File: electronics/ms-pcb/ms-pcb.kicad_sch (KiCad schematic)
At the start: 20 parts, among them J1 Left motor, J2 Right motor, J3 XT60-M, U1 ESP32-S3-DEVKITC-1U-N8R2, U2 GY-521

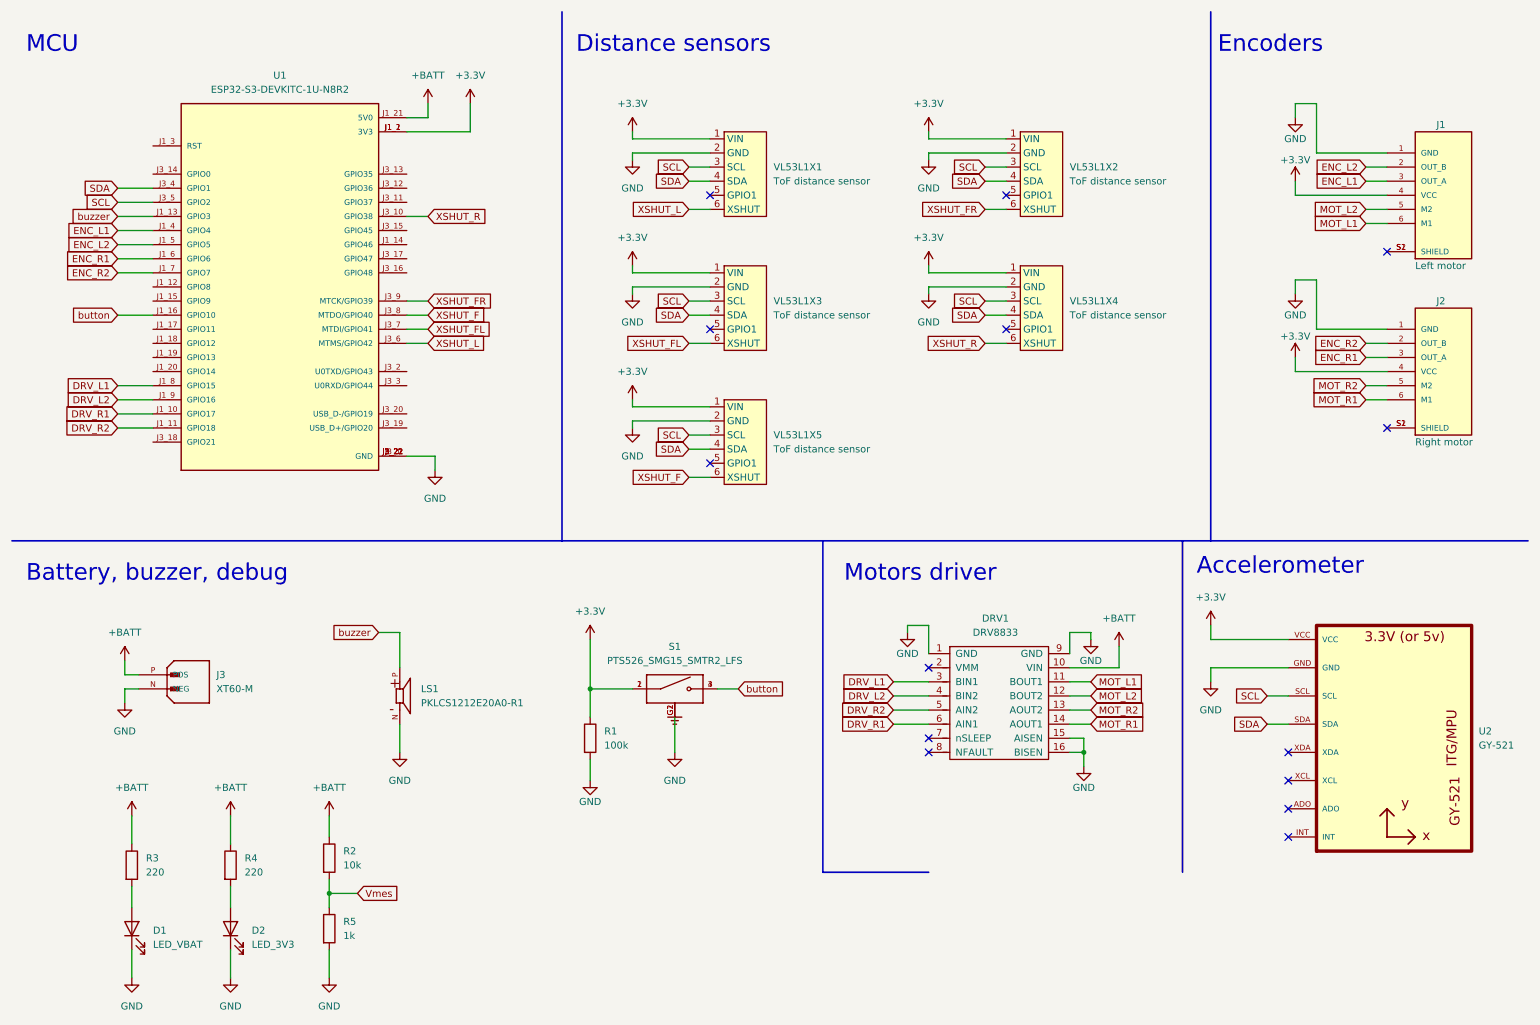
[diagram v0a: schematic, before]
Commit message: elec: start PCB layout
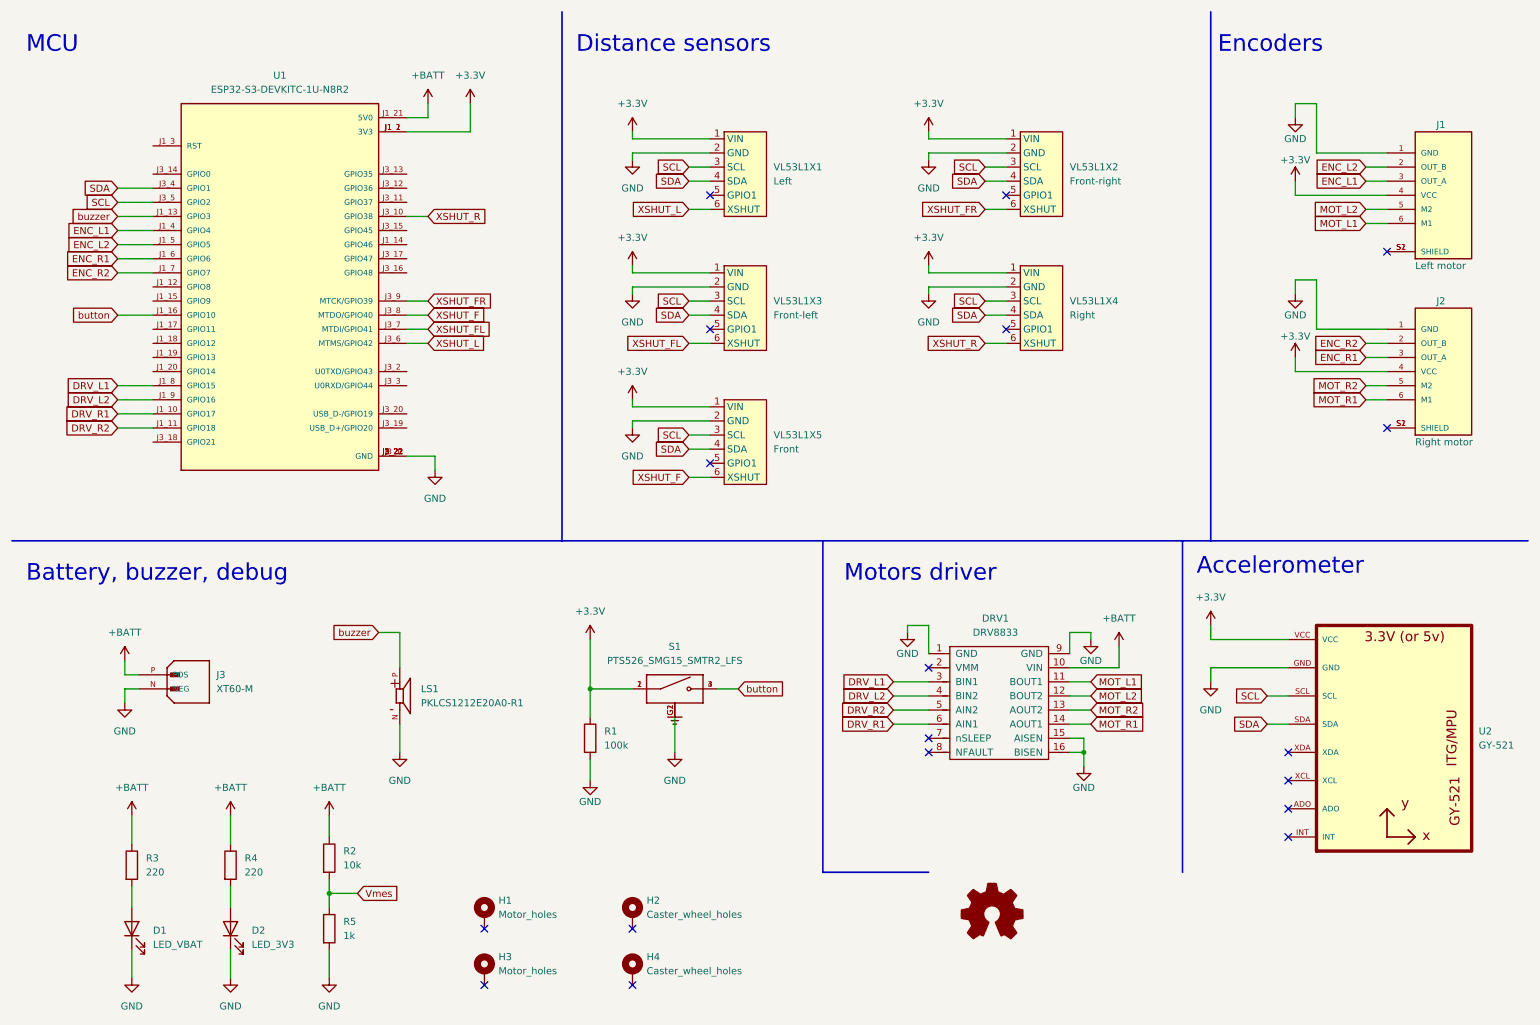
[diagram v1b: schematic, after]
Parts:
- added H1, H3: Motor_holes, footprints:Polulu_Micro_Gearmotor, symbol Mechanical:MountingHole_Pad
- added H2, H4: Caster_wheel_holes, footprints:caster_wheel, symbol Mechanical:MountingHole_Pad
- D1, D2: footprint (none) -> LED_SMD:LED_1206_3216Metric_Pad1.42x1.75mm_HandSolder
- J1, J2: footprint BM06B-SRSS-TB_LF__SN_:JST_BM06B-SRSS-TB_LF__SN_ -> footprints:JST_SH_6pins
- J3: footprint XT60-M:AMASS_XT60-M -> footprints:AMASS_XT60-M
- LS1: footprint PKLCS1212E20A0-R1:SPKR_PKLCS1212E20A0-R1 -> footprints:SPKR_PKLCS1212E20A0-R1
- R1, R2, R3, R4, R5: footprint (none) -> Resistor_SMD:R_1206_3216Metric_Pad1.30x1.75mm_HandSolder
- S1: footprint PTS526_SMG15_SMTR2_LFS:SW_PTS526_SMG15_SMTR2_LFS -> footprints:SW_PTS526_SMG15_SMTR2_LFS
- U1: footprint ESP32-S3-DEVKITC-1U-N8R2:XCVR_ESP32-S3-DEVKITC-1U-N8R2 -> footprints:XCVR_ESP32-S3-DEVKITC-1U-N8R2
- U2: footprint GY-521:GY-521 -> footprints:GY-521
- VL53L1X1: value ToF distance sensor -> Left; footprint (none) -> footprints:TinyTronics_VL53L1X
- VL53L1X2: value ToF distance sensor -> Front-right; footprint (none) -> footprints:TinyTronics_VL53L1X
- VL53L1X3: value ToF distance sensor -> Front-left; footprint (none) -> footprints:TinyTronics_VL53L1X
- VL53L1X4: value ToF distance sensor -> Right; footprint (none) -> footprints:TinyTronics_VL53L1X
- VL53L1X5: value ToF distance sensor -> Front; footprint (none) -> footprints:TinyTronics_VL53L1X
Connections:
- no-connect marks 14 -> 18

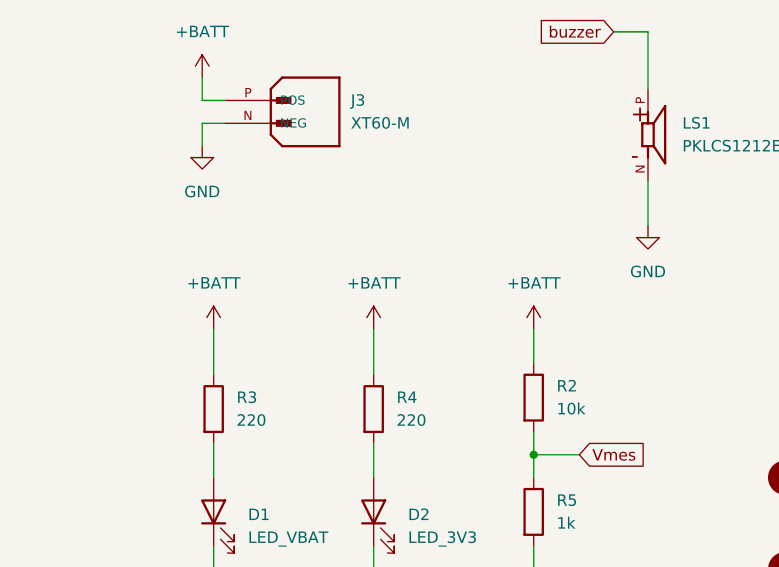
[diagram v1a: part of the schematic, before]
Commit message: elec: minor schematic fixes
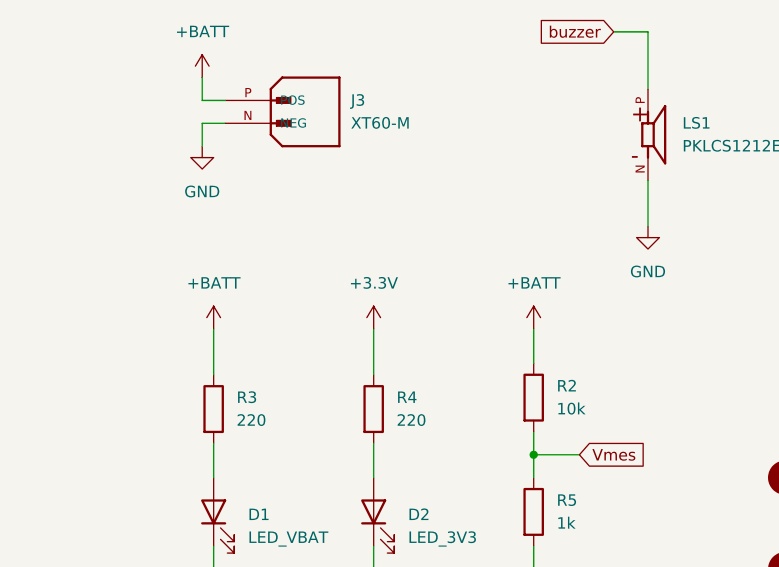
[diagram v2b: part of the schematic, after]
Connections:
- net +3.3V: now also R4.1
- net +BATT: no longer R4.1
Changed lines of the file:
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@@
     (pin "P")
-  )
-  (symbol (lib_id "power:+BATT") (at 50.8 156.21 0) (unit 1)
-    (in_bom yes) (on_board yes)
-    (property "Reference" "#PWR031" (id 0) (at 50.8 160.02 0)
-      (effects (font (size 1.27 1.27)) hide)
-    )
-    (property "Value" "+BATT" (id 1) (at 50.8 151.13 0))
-    (property "Footprint" "" (id 2) (at 50.8 156.21 0)
-      (effects (font (size 1.27 1.27)) hide)
-    )
-    (property "Datasheet" "" (id 3) (at 50.8 156.21 0)
-      (effects (font (size 1.27 1.27)) hide)
-    )
-    (pin "1")
   )
   (symbol (lib_id "power:GND") (at 176.53 62.23 0) (unit 1)
@@
     )
     (property "Datasheet" "" (id 3) (at 242.57 41.91 0)
+      (effects (font (size 1.27 1.27)) hide)
+    )
+    (pin "1")
+  )
+  (symbol (lib_id "power:+3.3V") (at 50.8 156.21 0) (unit 1)
+    (in_bom yes) (on_board yes) (fields_autoplaced)
+    (property "Reference" "#PWR?" (id 0) (at 50.8 160.02 0)
+      (effects (font (size 1.27 1.27)) hide)
+    )
+    (property "Value" "+3.3V" (id 1) (at 50.8 151.13 0))
+    (property "Footprint" "" (id 2) (at 50.8 156.21 0)
+      (effects (font (size 1.27 1.27)) hide)
+    )
+    (property "Datasheet" "" (id 3) (at 50.8 156.21 0)
       (effects (font (size 1.27 1.27)) hide)
     )
@@
       (reference "#PWR030") (unit 1) (value "+BATT") (footprint "")
     )
-    (path "/9c46dd07-06c6-44d5-9650-1b2bc80123b8"
-      (reference "#PWR031") (unit 1) (value "+BATT") (footprint "")
-    )
     (path "/40881dde-43ab-4252-b599-23e6f5bf1d52"
       (reference "#PWR032") (unit 1) (value "+BATT") (footprint "")
@@
       (reference "#PWR035") (unit 1) (value "GND") (footprint "")
     )
+    (path "/b021273c-faa8-417a-a42d-60ad91fbbbdf"
+      (reference "#PWR?") (unit 1) (value "+3.3V") (footprint "")
+    )
     (path "/640f477c-349e-4544-8313-0567779ba460"

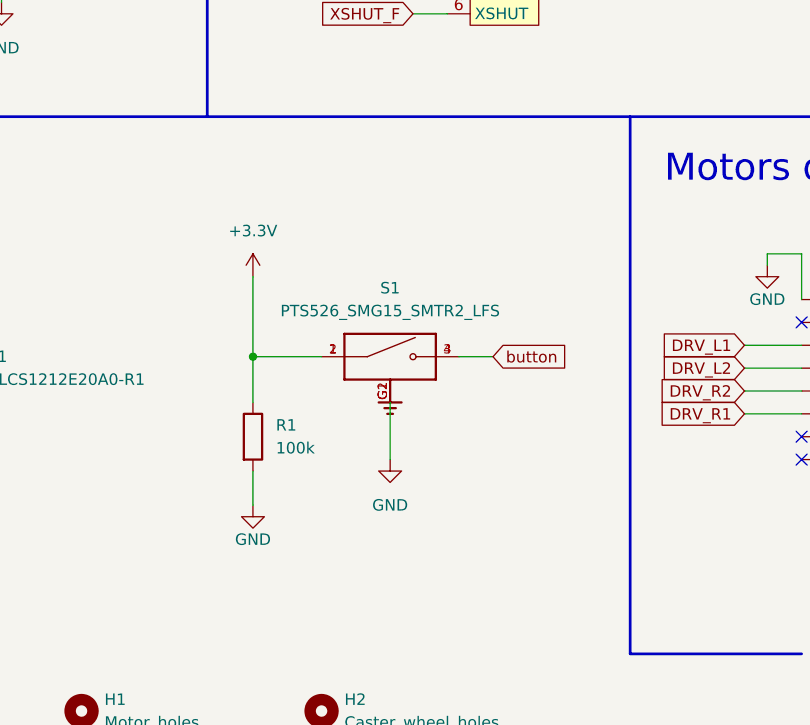
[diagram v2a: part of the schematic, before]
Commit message: elec: add more 3D and link them to footprints
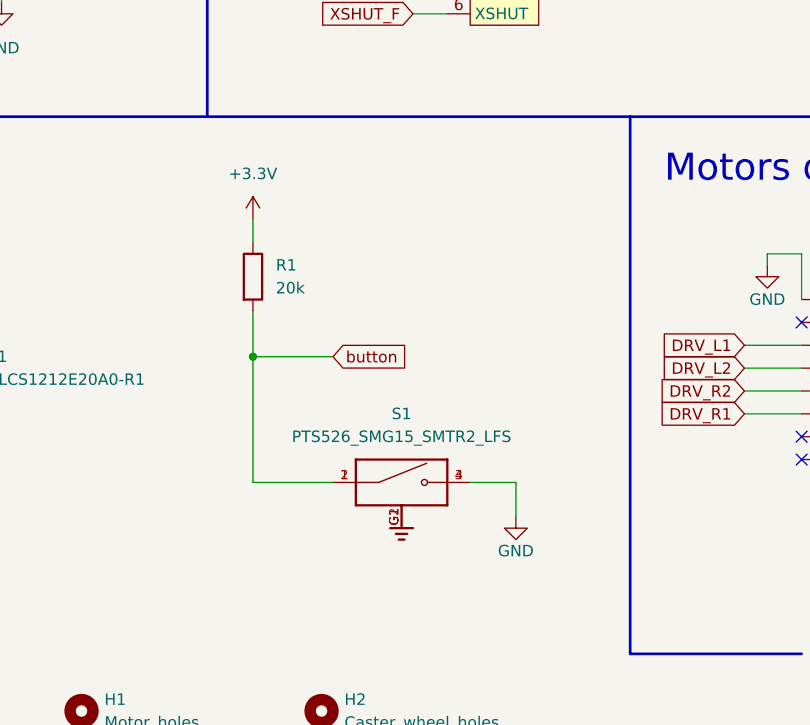
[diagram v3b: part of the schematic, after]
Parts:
- R1: value 100k -> 20k
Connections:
- net +3.3V: no longer S1.1, S1.2
- net GND: now also S1.3, S1.4; no longer R1.2, S1.G1, S1.G2
- net button: now also R1.2, S1.1, S1.2; no longer S1.3, S1.4
- new net: S1.G1, S1.G2
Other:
- moved on the sheet: R1, S1

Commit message: elec: add most 3D models
Closes: #19
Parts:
- DRV1: footprint (none) -> footprints:Polulu_DRV8833
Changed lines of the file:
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@@
     (property "Reference" "DRV1" (id 0) (at 188.5569 120.65 0))
     (property "Value" "DRV8833" (id 1) (at 188.5569 123.19 0))
-    (property "Footprint" "" (id 2) (at 184.15 134.62 0)
+    (property "Footprint" "footprints:Polulu_DRV8833" (id 2) (at 184.15 134.62 0)
       (effects (font (size 1.27 1.27)) hide)
     )
@@
   (symbol (lib_id "power:+3.3V") (at 50.8 156.21 0) (unit 1)
     (in_bom yes) (on_board yes) (fields_autoplaced)
-    (property "Reference" "#PWR?" (id 0) (at 50.8 160.02 0)
+    (property "Reference" "#PWR0101" (id 0) (at 50.8 160.02 0)
       (effects (font (size 1.27 1.27)) hide)
     )
@@
     )
     (path "/b021273c-faa8-417a-a42d-60ad91fbbbdf"
-      (reference "#PWR?") (unit 1) (value "+3.3V") (footprint "")
+      (reference "#PWR0101") (unit 1) (value "+3.3V") (footprint "")
     )
     (path "/640f477c-349e-4544-8313-0567779ba460"
@@
     )
     (path "/8a807ff6-0a61-4154-9000-caf05d86c07b"
-      (reference "DRV1") (unit 1) (value "DRV8833") (footprint "")
+      (reference "DRV1") (unit 1) (value "DRV8833") (footprint "footprints:Polulu_DRV8833")
     )
     (path "/2e4ac29d-6732-4013-aa07-ad22438565d6"

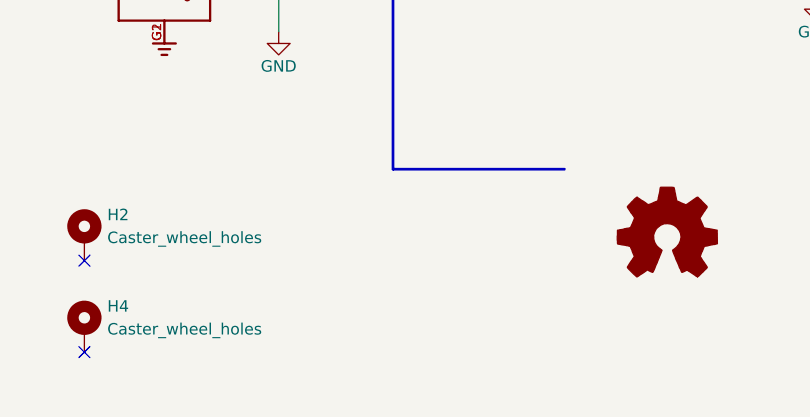
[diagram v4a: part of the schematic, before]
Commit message: elec: add more 3D models and enhance layout
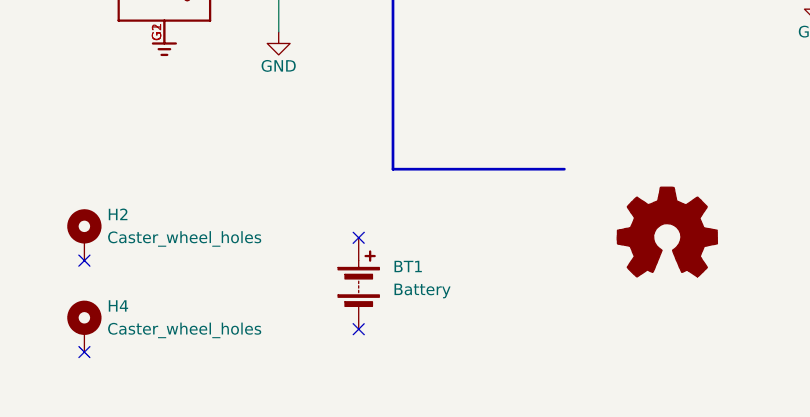
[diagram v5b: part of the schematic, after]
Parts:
- added BT1: Battery, footprints:LiPo_2S1P_Battery, symbol Device:Battery
- VL53L1X5: footprint footprints:TinyTronics_VL53L1X -> footprints:TinyTronics_VL53L1X_header_front
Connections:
- no-connect marks 18 -> 20

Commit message: elec: enhance PCB v0.1 layout
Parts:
- H2, H4: footprint footprints:caster_wheel -> footprints:caster_wheel_custom
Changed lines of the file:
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@@
 			)
 		)
-		(property "Description" ""
-			(at 256.54 139.7 0)
-			(effects
-				(font
-					(size 1.27 1.27)
-				)
-				(hide yes)
-			)
-		)
-		(property "MF" "GODREAM FORDREAM CO., LIMITED"
+		(property "Description" "\nTriple Axis Accelerometer Gyro Breakout\n"
 			(at 256.54 139.7 0)
 			(effects
@@
 			)
 		)
-		(property "Description" "\nTriple Axis Accelerometer Gyro Breakout\n"
+		(property "MF" "GODREAM FORDREAM CO., LIMITED"
 			(at 256.54 139.7 0)
 			(effects
@@
 			)
 		)
-		(property "Description" ""
-			(at 269.24 78.74 0)
+		(property "Description" "\nConnector Header Surface Mount 6 position 0.039 (1.00mm)\n"
+			(at 238.76 102.87 0)
 			(effects
 				(font
 					(size 1.27 1.27)
 				)
+				(justify bottom)
 				(hide yes)
 			)
@@
 			)
 		)
-		(property "Description" "\nConnector Header Surface Mount 6 position 0.039 (1.00mm)\n"
-			(at 238.76 102.87 0)
-			(effects
-				(font
-					(size 1.27 1.27)
-				)
-				(justify bottom)
-				(hide yes)
-			)
-		)
 		(property "MANUFACTURER" "JST Sales America Inc."
 			(at 238.76 102.87 0)
@@
 			)
 		)
-		(property "Description" ""
-			(at 269.24 46.99 0)
+		(property "Description" "\nConnector Header Surface Mount 6 position 0.039 (1.00mm)\n"
+			(at 238.76 71.12 0)
 			(effects
 				(font
 					(size 1.27 1.27)
 				)
+				(justify bottom)
 				(hide yes)
 			)
@@
 			)
 		)
-		(property "Description" "\nConnector Header Surface Mount 6 position 0.039 (1.00mm)\n"
-			(at 238.76 71.12 0)
-			(effects
-				(font
-					(size 1.27 1.27)
-				)
-				(justify bottom)
-				(hide yes)
-			)
-		)
 		(property "MANUFACTURER" "JST Sales America Inc."
 			(at 238.76 71.12 0)
@@
 			)
 		)
-		(property "Footprint" "footprints:caster_wheel"
+		(property "Footprint" "footprints:caster_wheel_custom"
 			(at 123.19 184.15 0)
 			(effects
@@
 			)
 		)
-		(property "Description" ""
+		(property "Description" "\nPlug; DC supply; XT60; male; PIN: 2; for cable; soldered; 30A; 500V\n"
 			(at 39.37 133.35 0)
 			(effects
@@
 					(size 1.27 1.27)
 				)
+				(justify bottom)
 				(hide yes)
 			)
@@
 			)
 		)
-		(property "Description" "\nPlug; DC supply; XT60; male; PIN: 2; for cable; soldered; 30A; 500V\n"
-			(at 39.37 133.35 0)
-			(effects
-				(font
-					(size 1.27 1.27)
-				)
-				(justify bottom)
-				(hide yes)
-			)
-		)
 		(property "Availability" "Not in stock"
 			(at 39.37 133.35 0)
@@
 			)
 		)
-		(property "Description" ""
+		(property "Description" "\nTactile Switch SPST-NO Top Actuated Surface Mount\n"
 			(at 132.08 147.32 0)
 			(effects
@@
 					(size 1.27 1.27)
 				)
+				(justify bottom)
 				(hide yes)
 			)
@@
 			)
 		)
-		(property "Description" "\nTactile Switch SPST-NO Top Actuated Surface Mount\n"
-			(at 132.08 147.32 0)
-			(effects
-				(font
-					(size 1.27 1.27)
-				)
-				(justify bottom)
-				(hide yes)
-			)
-		)
 		(property "Availability" "In Stock"
 			(at 132.08 147.32 0)
@@
 			)
 		)
-		(property "Description" ""
+		(property "Description" "\nWiFi Development Tools - 802.11 ESP32-S3 Gen-Purpose Dev Bd, embeds ESP32-S3-WROOM-1U-N8R2, 8 MB Quad Flash, 2 MB Quad PSRAM, IPEX antenna connector, w/ Pin Header\n"
 			(at 59.69 60.96 0)
 			(effects
@@
 					(size 1.27 1.27)
 				)
+				(justify bottom)
 				(hide yes)
 			)
@@
 			)
 		)
-		(property "Description" "\nWiFi Development Tools - 802.11 ESP32-S3 Gen-Purpose Dev Bd, embeds ESP32-S3-WROOM-1U-N8R2, 8 MB Quad Flash, 2 MB Quad PSRAM, IPEX antenna connector, w/ Pin Header\n"
-			(at 59.69 60.96 0)
-			(effects
-				(font
-					(size 1.27 1.27)
-				)
-				(justify bottom)
-				(hide yes)
-			)
-		)
 		(property "Availability" "In Stock"
 			(at 59.69 60.96 0)
@@
 			)
 		)
-		(property "Footprint" "footprints:caster_wheel"
+		(property "Footprint" "footprints:caster_wheel_custom"
 			(at 123.19 173.99 0)
 			(effects
@@
 			)
 		)
-		(property "Description" ""
+		(property "Description" "\nBuzzers Transducer, Externally Driven Piezo 1.5 V - 2kHz 70dB @ 1.5V, 10cm Surface Mount Solder Pads\n"
 			(at 81.28 134.62 0)
 			(effects
@@
 					(size 1.27 1.27)
 				)
+				(justify bottom)
 				(hide yes)
 			)
@@
 			(at 81.28 134.62 0)
 			(effects
-				(font
-					(size 1.27 1.27)
-				)
-				(justify bottom)
-				(hide yes)
-			)
-		)
-		(property "Description" "\nBuzzers Transducer, Externally Driven Piezo 1.5 V - 2kHz 70dB @ 1.5V, 10cm Surface Mount Solder Pads\n"
-			(at 81.28 134.62 0)
-			(effects
